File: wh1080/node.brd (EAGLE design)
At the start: 50 x 24 mm, 5 parts, among them J1 AVR_SPI_PRG_62X3_LOCK

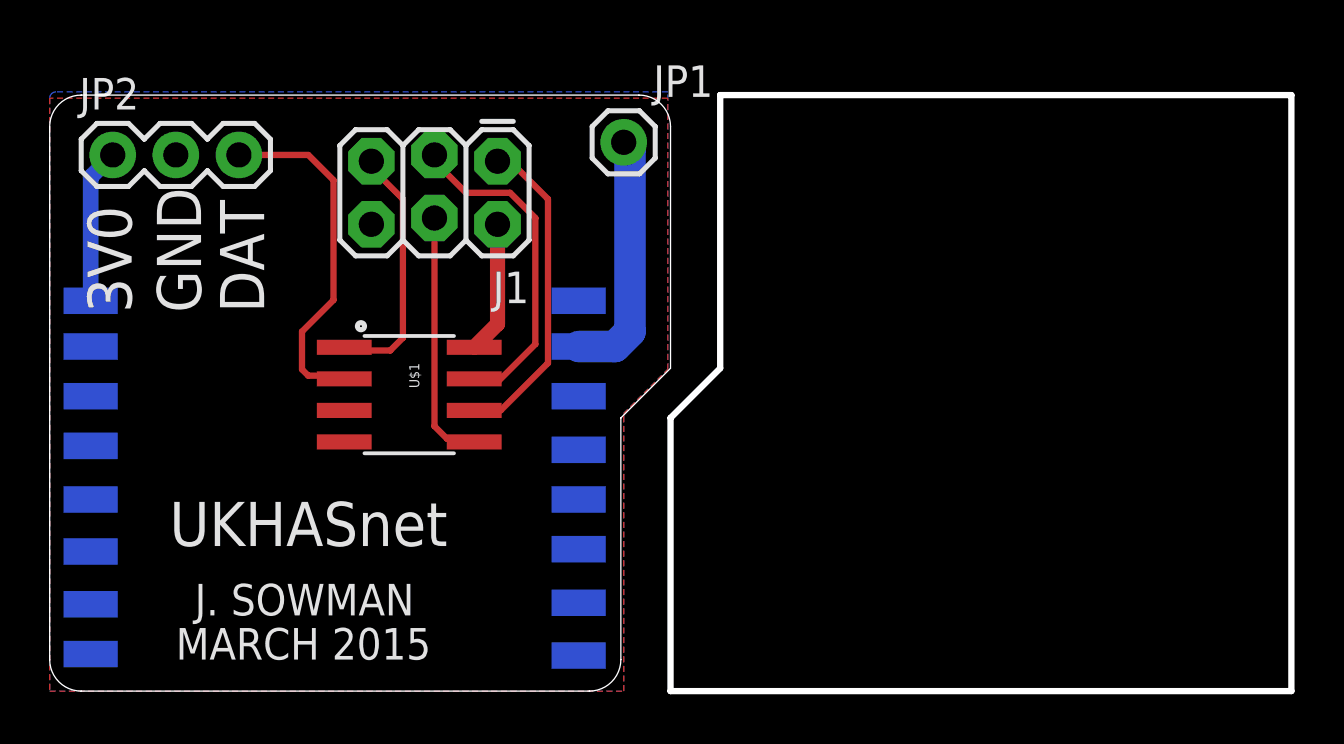
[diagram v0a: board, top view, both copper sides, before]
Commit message: routed wh1080 txer
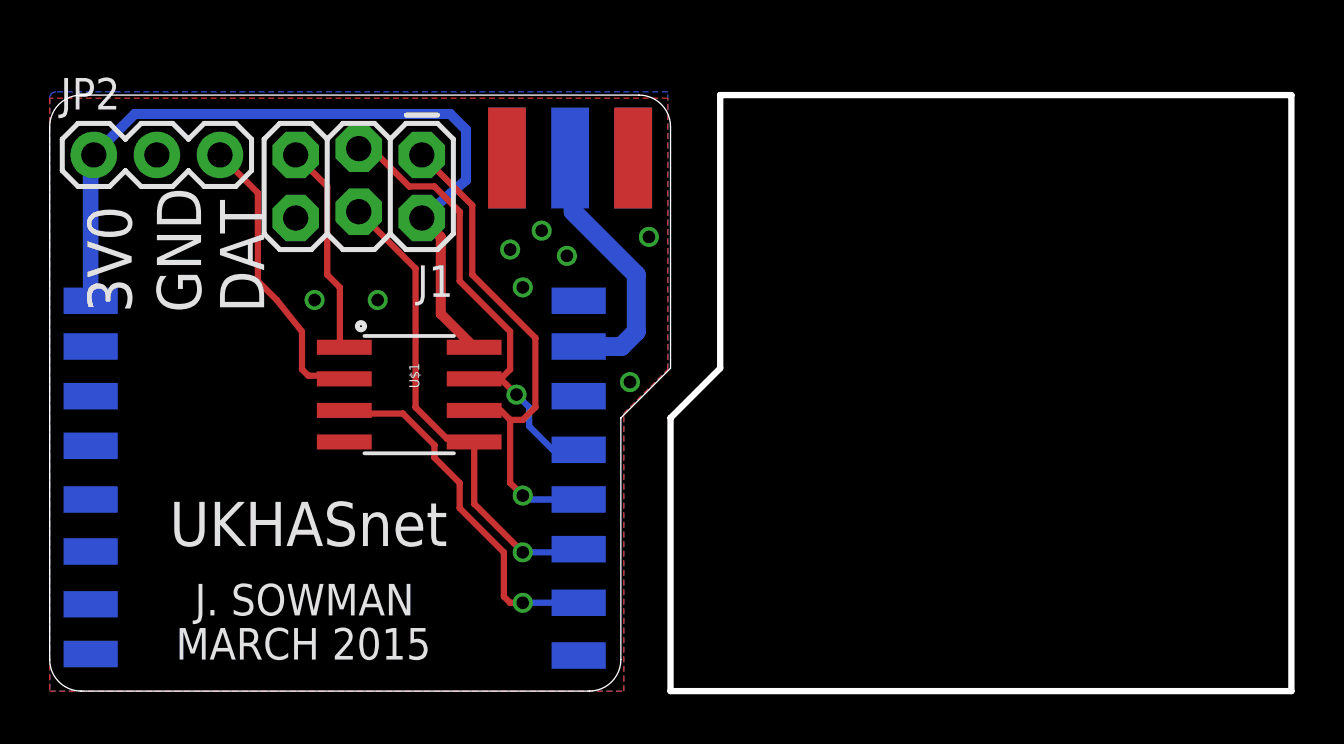
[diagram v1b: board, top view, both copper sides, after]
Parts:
- removed JP1: M01PTH, SparkFun-Connectors:1X01
- added J$1: SMA_EDGE, jonsowman:SMA-EDGE
- moved J1 3.06 mm to (15.0, 21.6)
- moved JP2 0.76 mm to (1.78, 21.6)
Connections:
- removed net N$3: JP1.1, U$4.ANT
- new net N$1: J$1.SIG, U$4.ANT
- net GND: now also J$1.GND@0, J$1.GND@1, J$1.GND@2, J$1.GND@3
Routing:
- net VCC: track 11.6 -> 32.3 mm
- net RFM_SS: track 0.00 -> 14.6 mm, vias 0 -> 1
- net N$1: track 0.00 -> 10.7 mm
- net N$3: track 10.0 -> 0.00 mm
- net MOSI: track 10.2 -> 19.3 mm, vias 0 -> 1
- net MISO: track 13.0 -> 20.5 mm, vias 0 -> 1
- net SCK: track 13.5 -> 18.8 mm, vias 0 -> 1
- net DATA: track 14.2 -> 11.8 mm
- net RESET: track 10.3 -> 8.84 mm
